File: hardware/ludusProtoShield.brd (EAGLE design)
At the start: 59.7 x 53.3 mm, 54 parts, among them U1 ARDUINO, U2 TB6612FNG

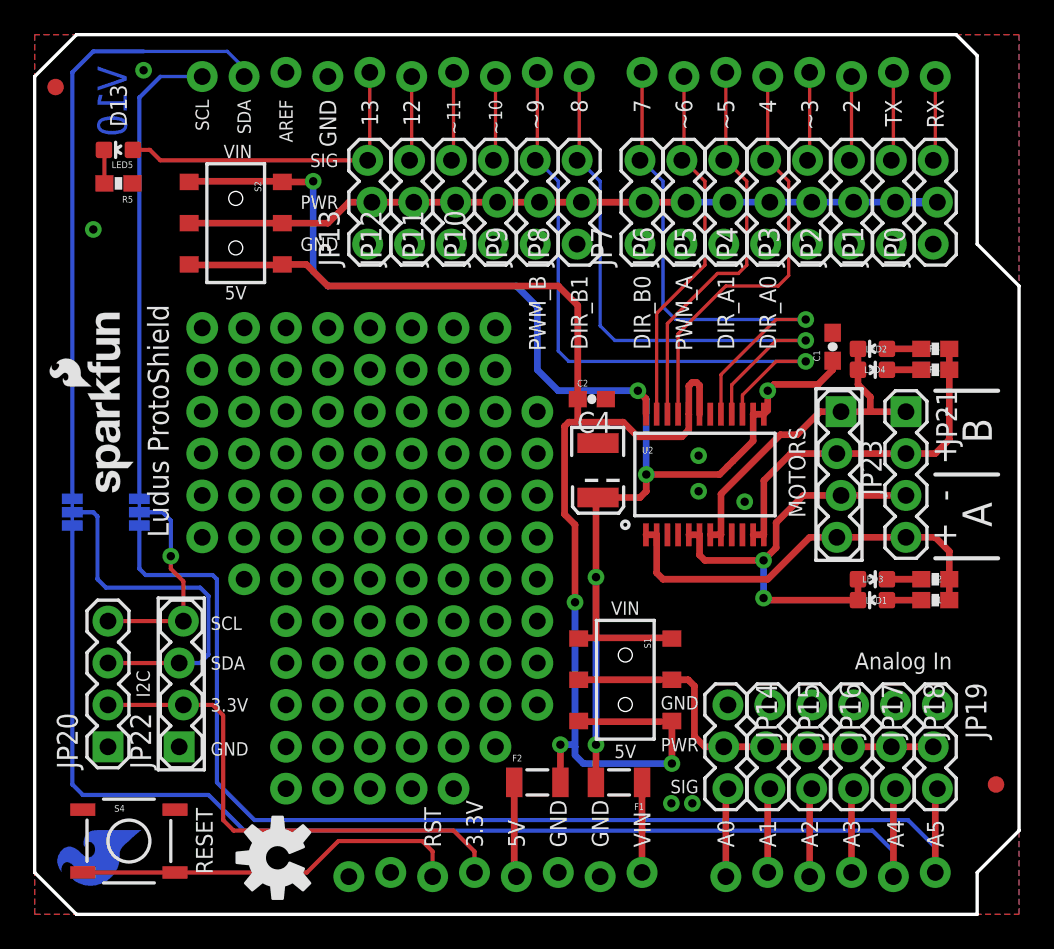
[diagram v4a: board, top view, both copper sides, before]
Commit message: Added QC testpoints to board
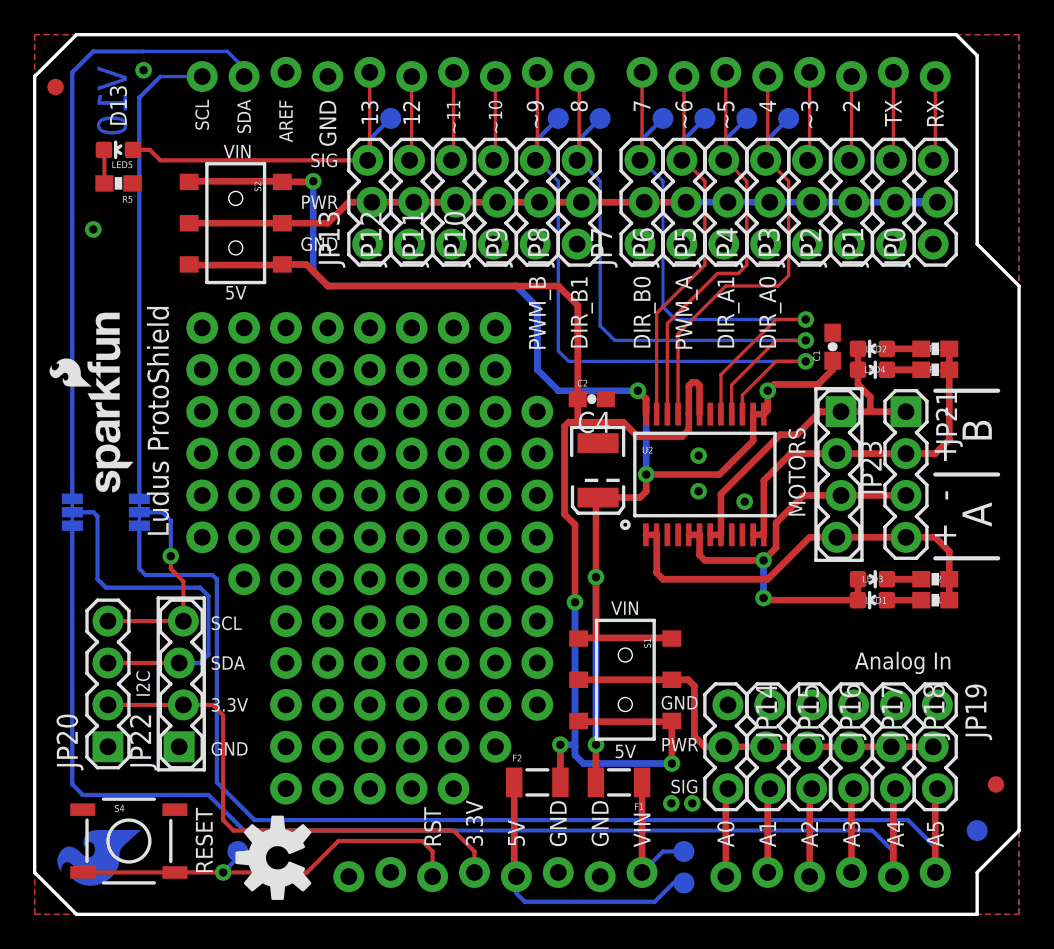
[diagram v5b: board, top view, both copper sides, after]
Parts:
- added TP1, TP10, TP11, TP2, TP3, TP4, TP5, TP6, TP7, TP8, TP9: (no value), SparkFun-Passives:PAD.03X.05
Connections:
- net AIN1: now also TP1.P$1
- net AIN2: now also TP2.P$1
- net BIN1: now also TP4.P$1
- net BIN2: now also TP5.P$1
- net D13: now also TP7.P$1
- net GND: now also TP11.P$1
- net PWMA: now also TP3.P$1
- net PWMB: now also TP6.P$1
- net RESET: now also TP8.P$1
- net VCC: now also TP10.P$1
- net VIN: now also TP9.P$1
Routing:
- net VCC: track 5.77 -> 17.6 mm
- net PWMB: track 38.7 -> 41.8 mm
- net PWMA: track 22.4 -> 25.5 mm
- net D13: track 19.9 -> 23.0 mm
- net BIN2: track 36.0 -> 39.2 mm
- net BIN1: track 32.8 -> 35.9 mm
- net AIN2: track 24.2 -> 27.3 mm
- net AIN1: track 25.8 -> 28.9 mm
- net VIN: track 5.46 -> 8.53 mm
- net RESET: track 23.8 -> 25.4 mm, vias 0 -> 1
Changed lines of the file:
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@@
 <layer number="23" name="tOrigins" color="15" fill="1" visible="yes" active="yes"/>
 <layer number="24" name="bOrigins" color="15" fill="1" visible="yes" active="yes"/>
-<layer number="25" name="tNames" color="7" fill="1" visible="no" active="yes"/>
-<layer number="26" name="bNames" color="7" fill="1" visible="no" active="yes"/>
+<layer number="25" name="tNames" color="7" fill="1" visible="yes" active="yes"/>
+<layer number="26" name="bNames" color="7" fill="1" visible="yes" active="yes"/>
 <layer number="27" name="tValues" color="7" fill="1" visible="no" active="yes"/>
 <layer number="28" name="bValues" color="7" fill="1" visible="no" active="yes"/>
@@
 <layer number="45" name="Holes" color="7" fill="1" visible="no" active="yes"/>
 <layer number="46" name="Milling" color="3" fill="1" visible="no" active="yes"/>
-<layer number="51" name="tDocu" color="6" fill="1" visible="yes" active="yes"/>
+<layer number="51" name="tDocu" color="6" fill="1" visible="no" active="yes"/>
 <layer number="52" name="bDocu" color="7" fill="1" visible="no" active="yes"/>
 <layer number="2" name="Route2" color="1" fill="3" visible="no" active="no"/>
@@
 <element name="U$1" library="SparkFun-Aesthetics" package="SFE_LUDUS-M" value="SFE_LUDUSSFE_LUDUS-M" x="41.275" y="26.67" rot="SMR270"/>
 <element name="LOGO3" library="SparkFun-Aesthetics" package="SFE_LOGO_FLAME_COPPER_.2" value="SFE_LOGO_FLAME.2COP" x="6.731" y="5.461" rot="MR270"/>
+<element name="TP2" library="SparkFun-Passives" package="PAD.03X.05" value="" x="43.18" y="48.26" rot="MR0"/>
+<element name="TP1" library="SparkFun-Passives" package="PAD.03X.05" value="" x="45.72" y="48.26" rot="MR0"/>
+<element name="TP3" library="SparkFun-Passives" package="PAD.03X.05" value="" x="40.64" y="48.26" rot="MR0"/>
+<element name="TP6" library="SparkFun-Passives" package="PAD.03X.05" value="" x="31.75" y="48.26" rot="MR90"/>
+<element name="TP4" library="SparkFun-Passives" package="PAD.03X.05" value="" x="38.1" y="48.26" rot="MR90"/>
+<element name="TP5" library="SparkFun-Passives" package="PAD.03X.05" value="" x="34.29" y="48.26" rot="MR90"/>
+<element name="TP7" library="SparkFun-Passives" package="PAD.03X.05" value="" x="21.59" y="48.26" rot="MR90"/>
+<element name="TP8" library="SparkFun-Passives" package="PAD.03X.05" value="" x="12.319" y="3.81" rot="MR0"/>
+<element name="TP9" library="SparkFun-Passives" package="PAD.03X.05" value="" x="39.37" y="3.81" rot="MR90"/>
+<element name="TP10" library="SparkFun-Passives" package="PAD.03X.05" value="" x="39.37" y="1.905" rot="MR0"/>
+<element name="TP11" library="SparkFun-Passives" package="PAD.03X.05" value="" x="57.15" y="5.08" rot="MR0"/>
 </elements>
 <signals>
@@
 <via x="3.556" y="41.529" extent="1-16" drill="0.508"/>
 <via x="6.604" y="51.181" extent="1-16" drill="0.508"/>
+<contactref element="TP11" pad="P$1"/>
 </signal>
 <signal name="D12">
@@
 <wire x1="20.32" y1="51.054" x2="20.32" y2="45.847" width="0.2032" layer="1"/>
 <wire x1="20.32" y1="45.847" x2="20.193" y2="45.72" width="0.2032" layer="1"/>
+<contactref element="TP7" pad="P$1"/>
+<wire x1="21.59" y1="48.26" x2="20.32" y2="46.99" width="0.254" layer="16"/>
+<wire x1="20.32" y1="46.99" x2="20.32" y2="45.847" width="0.254" layer="16"/>
+<wire x1="20.32" y1="45.847" x2="20.193" y2="45.72" width="0.254" layer="16"/>
 </signal>
 <signal name="PWMA">
@@
 <wire x1="39.243" y1="45.72" x2="39.37" y2="45.72" width="0.2032" layer="1"/>
 <wire x1="39.37" y1="45.72" x2="40.64" y2="44.45" width="0.2032" layer="1"/>
+<contactref element="TP3" pad="P$1"/>
+<wire x1="40.64" y1="48.26" x2="39.37" y2="46.99" width="0.254" layer="16"/>
+<wire x1="39.37" y1="46.99" x2="39.37" y2="45.847" width="0.254" layer="16"/>
+<wire x1="39.37" y1="45.847" x2="39.243" y2="45.72" width="0.254" layer="16"/>
 </signal>
 <signal name="PWMB">
@@
 <wire x1="30.353" y1="45.72" x2="30.48" y2="45.72" width="0.2032" layer="16"/>
 <wire x1="30.48" y1="45.72" x2="31.75" y2="44.45" width="0.2032" layer="16"/>
+<contactref element="TP6" pad="P$1"/>
+<wire x1="31.75" y1="48.26" x2="30.48" y2="46.99" width="0.254" layer="16"/>
+<wire x1="30.48" y1="46.99" x2="30.48" y2="45.847" width="0.254" layer="16"/>
+<wire x1="30.48" y1="45.847" x2="30.353" y2="45.72" width="0.254" layer="16"/>
 </signal>
 <signal name="VIN">
@@
 <wire x1="36.83" y1="2.54" x2="36.83" y2="7.998" width="0.4064" layer="1"/>
 <wire x1="36.83" y1="7.998" x2="36.833" y2="8.001" width="0.4064" layer="1"/>
+<contactref element="TP9" pad="P$1"/>
+<wire x1="39.37" y1="3.81" x2="38.1" y2="3.81" width="0.254" layer="16"/>
+<wire x1="38.1" y1="3.81" x2="36.83" y2="2.54" width="0.254" layer="16"/>
 </signal>
 <signal name="N$4">
@@
 <wire x1="29.08" y1="8.001" x2="29.08" y2="2.416" width="0.4064" layer="1"/>
 <wire x1="29.08" y1="2.416" x2="29.21" y2="2.286" width="0.4064" layer="1"/>
+<contactref element="TP10" pad="P$1"/>
+<wire x1="39.37" y1="1.905" x2="38.735" y2="1.905" width="0.254" layer="16"/>
+<wire x1="38.735" y1="1.905" x2="37.592" y2="0.762" width="0.254" layer="16"/>
+<wire x1="37.592" y1="0.762" x2="29.718" y2="0.762" width="0.254" layer="16"/>
+<wire x1="29.718" y1="0.762" x2="29.21" y2="1.27" width="0.254" layer="16"/>
+<wire x1="29.21" y1="1.27" x2="29.21" y2="2.286" width="0.254" layer="16"/>
 </signal>
 <signal name="D10">
@@
 <wire x1="36.83" y1="45.72" x2="38.1" y2="44.45" width="0.2032" layer="16"/>
 <wire x1="46.755" y1="36.068" x2="44.958" y2="36.068" width="0.2032" layer="1"/>
+<contactref element="TP4" pad="P$1"/>
+<wire x1="38.1" y1="48.26" x2="36.83" y2="46.99" width="0.254" layer="16"/>
+<wire x1="36.83" y1="46.99" x2="36.83" y2="45.847" width="0.254" layer="16"/>
+<wire x1="36.83" y1="45.847" x2="36.703" y2="45.72" width="0.254" layer="16"/>
 </signal>
 <signal name="AIN2">
@@
 <wire x1="41.783" y1="45.72" x2="41.91" y2="45.72" width="0.2032" layer="1"/>
 <wire x1="41.91" y1="45.72" x2="43.18" y2="44.45" width="0.2032" layer="1"/>
+<contactref element="TP2" pad="P$1"/>
+<wire x1="43.18" y1="48.26" x2="41.91" y2="46.99" width="0.254" layer="16"/>
+<wire x1="41.91" y1="46.99" x2="41.91" y2="45.847" width="0.254" layer="16"/>
+<wire x1="41.91" y1="45.847" x2="41.783" y2="45.72" width="0.254" layer="16"/>
 </signal>
 <signal name="AIN1">
@@
 <wire x1="44.323" y1="45.72" x2="44.45" y2="45.72" width="0.2032" layer="1"/>
 <wire x1="44.45" y1="45.72" x2="45.72" y2="44.45" width="0.2032" layer="1"/>
+<contactref element="TP1" pad="P$1"/>
+<wire x1="45.72" y1="48.26" x2="44.45" y2="46.99" width="0.254" layer="16"/>
+<wire x1="44.45" y1="46.99" x2="44.45" y2="45.847" width="0.254" layer="16"/>
+<wire x1="44.45" y1="45.847" x2="44.323" y2="45.72" width="0.254" layer="16"/>
 </signal>
 <signal name="D11">
@@
 <contactref element="S4" pad="3"/>
 <wire x1="8.509" y1="2.54" x2="2.921" y2="2.54" width="0.254" layer="1"/>
-<wire x1="8.509" y1="2.54" x2="16.51" y2="2.54" width="0.254" layer="1"/>
+<wire x1="11.43" y1="2.54" x2="16.51" y2="2.54" width="0.254" layer="1"/>
 <wire x1="24.13" y1="3.81" x2="24.13" y2="2.286" width="0.254" layer="1"/>
 <wire x1="24.13" y1="3.81" x2="23.495" y2="4.445" width="0.254" layer="1"/>
 <wire x1="23.495" y1="4.445" x2="18.415" y2="4.445" width="0.254" layer="1"/>
 <wire x1="18.415" y1="4.445" x2="16.51" y2="2.54" width="0.254" layer="1"/>
+<contactref element="TP8" pad="P$1"/>
+<wire x1="12.319" y1="3.81" x2="12.319" y2="3.429" width="0.254" layer="16"/>
+<wire x1="12.319" y1="3.429" x2="11.43" y2="2.54" width="0.254" layer="16"/>
+<via x="11.43" y="2.54" extent="1-16" drill="0.508"/>
+<wire x1="11.43" y1="2.54" x2="8.509" y2="2.54" width="0.254" layer="1"/>
 </signal>
 <signal name="D3">
@@
 <wire x1="32.893" y1="45.72" x2="33.02" y2="45.72" width="0.2032" layer="16"/>
 <wire x1="33.02" y1="45.72" x2="34.29" y2="44.45" width="0.2032" layer="16"/>
+<contactref element="TP5" pad="P$1"/>
+<wire x1="34.29" y1="48.26" x2="33.02" y2="46.99" width="0.254" layer="16"/>
+<wire x1="33.02" y1="46.99" x2="33.02" y2="45.847" width="0.254" layer="16"/>
+<wire x1="33.02" y1="45.847" x2="32.893" y2="45.72" width="0.254" layer="16"/>
 </signal>
 <signal name="N$20">

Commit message: Nudged test points and fixed led prod_id for led 5
moved test points to avoid selective solder coverage and updated led 5
to include production id.
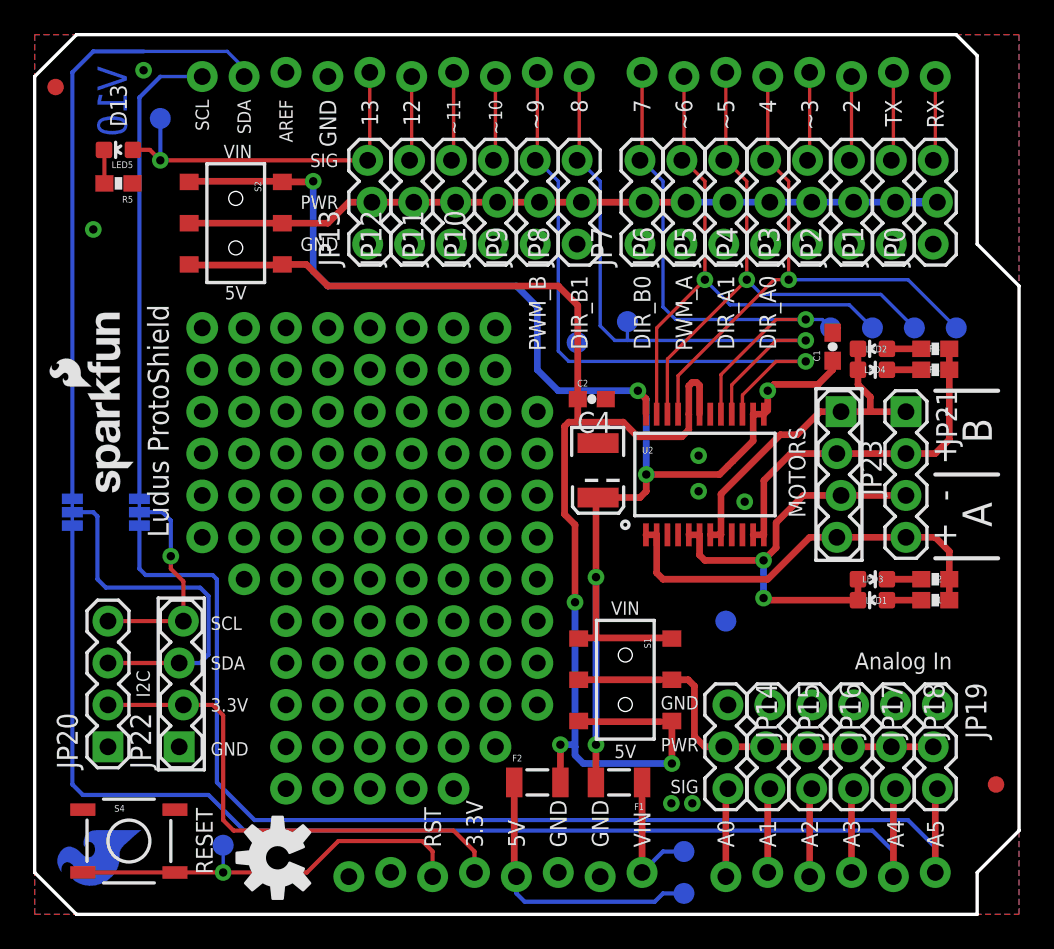
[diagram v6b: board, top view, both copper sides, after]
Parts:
- LED5: value Blue -> BLUE
- moved TP11 19.8 mm to (41.9, 17.8)
- moved TP1 16.3 mm to (55.9, 35.6)
- moved TP2 16.3 mm to (53.3, 35.6)
- moved TP3 16.3 mm to (50.8, 35.6)
- moved TP4 16.3 mm to (48.3, 35.6)
- moved TP7 14.0 mm to (7.62, 48.3)
- moved TP6 13.6 mm to (32.9, 34.7)
- moved TP5 12.4 mm to (35.9, 35.9)
- moved TP8 0.97 mm to (11.4, 4.19)
- moved TP10 0.64 mm to (39.4, 1.27)
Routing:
- net PWMA: track 25.5 -> 33.8 mm, vias 0 -> 1
- net AIN2: track 27.3 -> 34.8 mm, vias 0 -> 1
- net AIN1: track 28.9 -> 35.8 mm, vias 0 -> 1
- net PWMB: track 41.8 -> 39.9 mm
- net BIN2: track 39.2 -> 37.2 mm
- net BIN1: track 35.9 -> 34.5 mm
- net D13: track 23.0 -> 22.4 mm, vias 0 -> 1
